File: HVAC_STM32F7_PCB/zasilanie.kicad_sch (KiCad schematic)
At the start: 20 parts, among them J1 DC_Jack_5.5x2.1mm, Q1 IRLML6402, SW1 SLW-1276864-4A-D, U1 LM2596S-5, U2 LM2596S-3.3

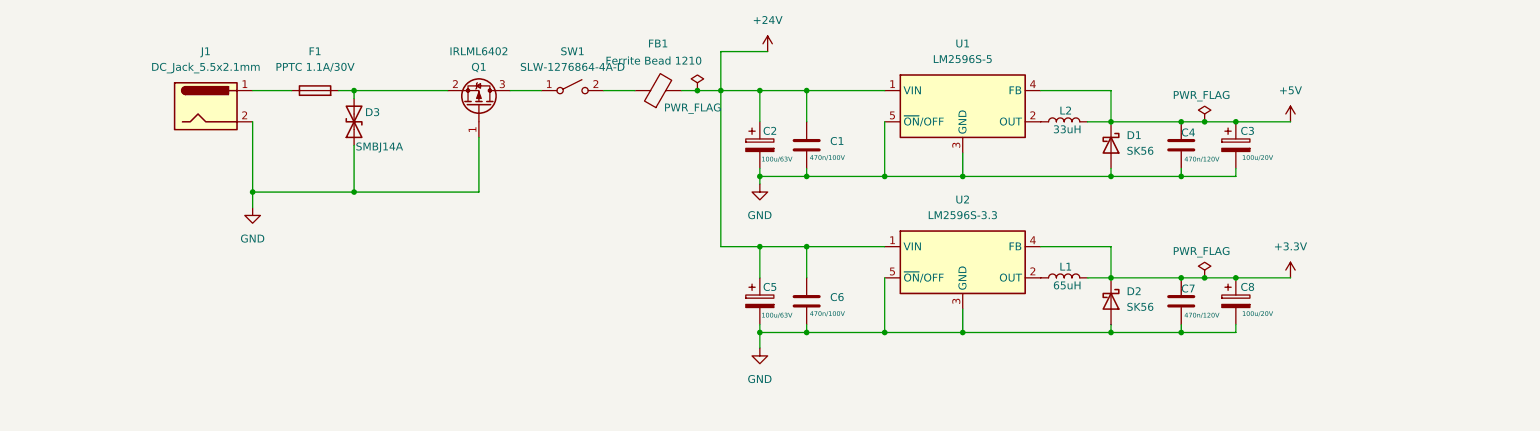
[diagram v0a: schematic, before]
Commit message: ADD: c-l-c filter, PMOS controll, inditacor LEDs, JLCPCB technology capabilities TODO: footprint assignment to lacking elements,
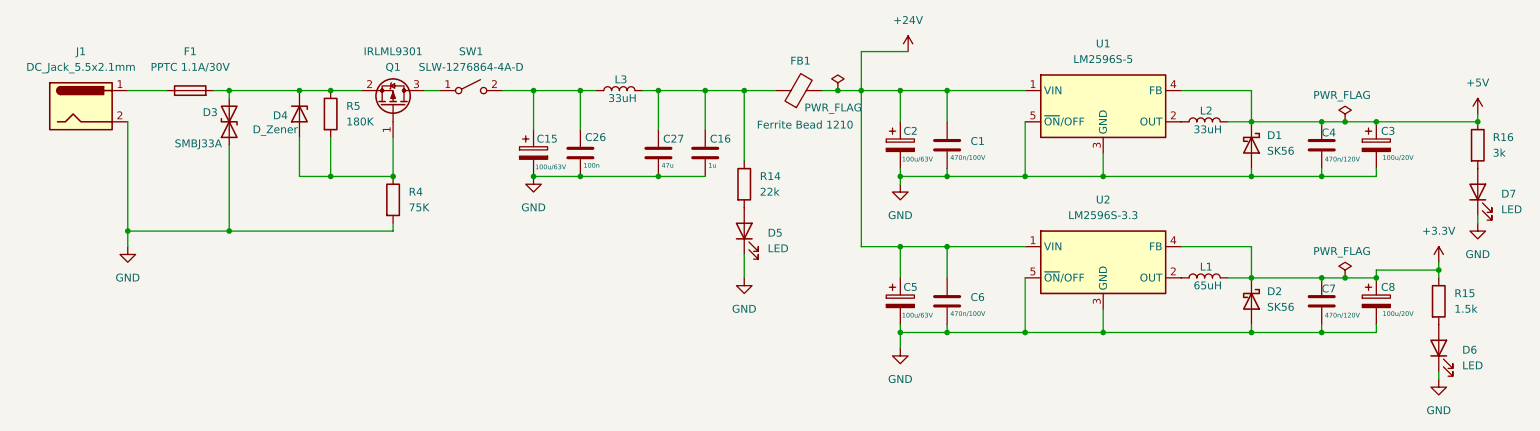
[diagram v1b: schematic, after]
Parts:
- added C15: 100u/63V, Capacitor_THT:CP_Radial_D8.0mm_P3.80mm, symbol Device:C_Polarized
- added C16: 1u, Capacitor_SMD:C_1808_4520Metric_Pad1.72x2.30mm_HandSolder, symbol Device:C
- added C26: 100n, Capacitor_SMD:C_1808_4520Metric_Pad1.72x2.30mm_HandSolder, symbol Device:C
- added C27: 47u, Capacitor_SMD:C_1808_4520Metric_Pad1.72x2.30mm_HandSolder, symbol Device:C
- added D4: D_Zener, symbol Device:D_Zener
- added D5, D6, D7: LED, symbol Device:LED
- added L3: 33uH, Inductor_SMD:L_6.3x6.3_H3, symbol Device:L
- added R14: 22k, Resistor_SMD:R_0805_2012Metric_Pad1.20x1.40mm_HandSolder, symbol Device:R
- added R15: 1.5k, Resistor_SMD:R_0805_2012Metric_Pad1.20x1.40mm_HandSolder, symbol Device:R
- added R16: 3k, Resistor_SMD:R_0805_2012Metric_Pad1.20x1.40mm_HandSolder, symbol Device:R
- added R4: 75K, Resistor_SMD:R_0805_2012Metric_Pad1.20x1.40mm_HandSolder, symbol Device:R
- added R5: 180K, Resistor_SMD:R_0805_2012Metric_Pad1.20x1.40mm_HandSolder, symbol Device:R
- D3: value SMBJ14A -> SMBJ33A; footprint Diode_SMD:D_SMB -> Diode_SMD:D_SMB_Handsoldering
- Q1: value IRLML6402 -> IRLML9301
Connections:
- net +3.3V: now also R15.1
- net +5V: now also R16.1
- net GND: now also C15.2, C16.2, C26.2, C27.2, D5.1 (K), D6.1 (K), D7.1 (K), R4.2; no longer Q1.1 (G)
- net at D3.2 (A2), F1.2, Q1.2 (S): now also D4.1 (K), R5.1
- net at SW1.2 (B): now also C15.1, C26.1, L3.1; no longer FB1.1
- new net: C16.1, C27.1, FB1.1, L3.2, R14.1
- new net: D7.2 (A), R16.2
- new net: D6.2 (A), R15.2
- new net: D4.2 (A), Q1.1 (G), R4.1, R5.2
- new net: D5.2 (A), R14.2
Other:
- moved on the sheet: C1, C2, C3, C4, C5, C6, C7, C8, D1, D2, D3, F1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
